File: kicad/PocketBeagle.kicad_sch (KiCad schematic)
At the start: 2 parts

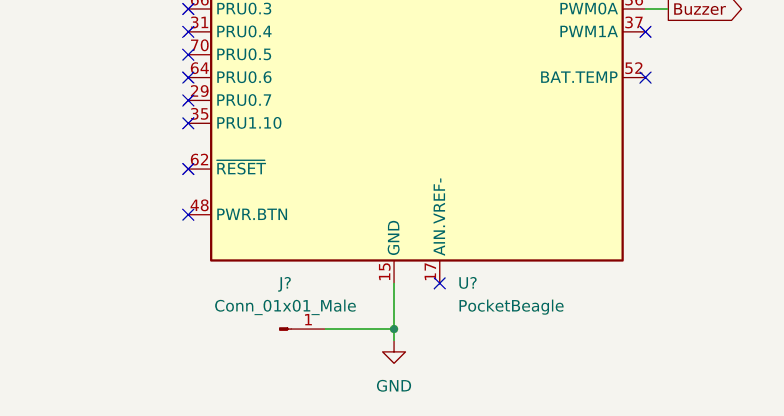
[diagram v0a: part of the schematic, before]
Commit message: Updated layout
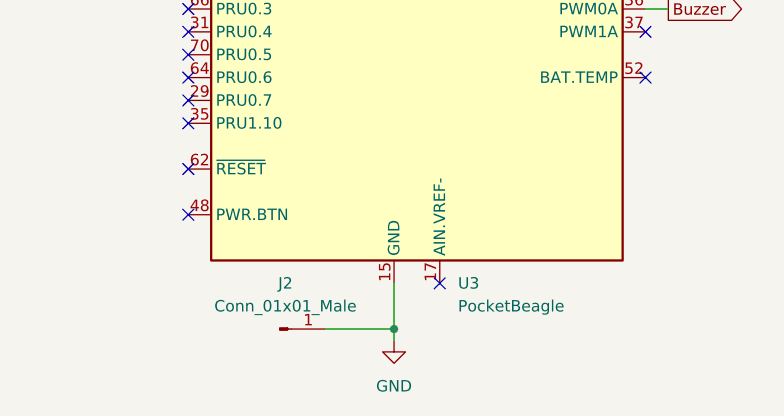
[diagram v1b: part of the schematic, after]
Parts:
- gave numbers to parts that had none: 2
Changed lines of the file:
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@@
   (symbol (lib_id "MCU_Module:PocketBeagle") (at 76.2 91.44 0) (unit 1)
     (in_bom yes) (on_board yes) (fields_autoplaced)
-    (property "Reference" "U?" (id 0) (at 80.7594 147.32 0)
+    (property "Reference" "U3" (id 0) (at 80.7594 147.32 0)
       (effects (font (size 1.27 1.27)) (justify left))
     )
@@
   (symbol (lib_id "Connector:Conn_01x01_Male") (at 60.96 152.4 0) (unit 1)
     (in_bom yes) (on_board yes)
-    (property "Reference" "J?" (id 0) (at 61.595 147.32 0))
+    (property "Reference" "J2" (id 0) (at 61.595 147.32 0))
     (property "Value" "Conn_01x01_Male" (id 1) (at 61.595 149.86 0))
     (property "Footprint" "Connector_PinHeader_2.54mm:PinHeader_1x01_P2.54mm_Vertical" (id 2) (at 60.96 152.4 0)
@@
   (symbol (lib_id "power:+3V3") (at 81.28 31.75 0) (mirror y) (unit 1)
     (in_bom yes) (on_board yes) (fields_autoplaced)
-    (property "Reference" "#PWR?" (id 0) (at 81.28 35.56 0)
+    (property "Reference" "#PWR08" (id 0) (at 81.28 35.56 0)
       (effects (font (size 1.27 1.27)) hide)
     )
@@
   (symbol (lib_id "power:GND") (at 73.66 153.67 0) (unit 1)
     (in_bom yes) (on_board yes) (fields_autoplaced)
-    (property "Reference" "#PWR?" (id 0) (at 73.66 160.02 0)
+    (property "Reference" "#PWR07" (id 0) (at 73.66 160.02 0)
       (effects (font (size 1.27 1.27)) hide)
     )
